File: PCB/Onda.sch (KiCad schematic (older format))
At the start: 0 parts

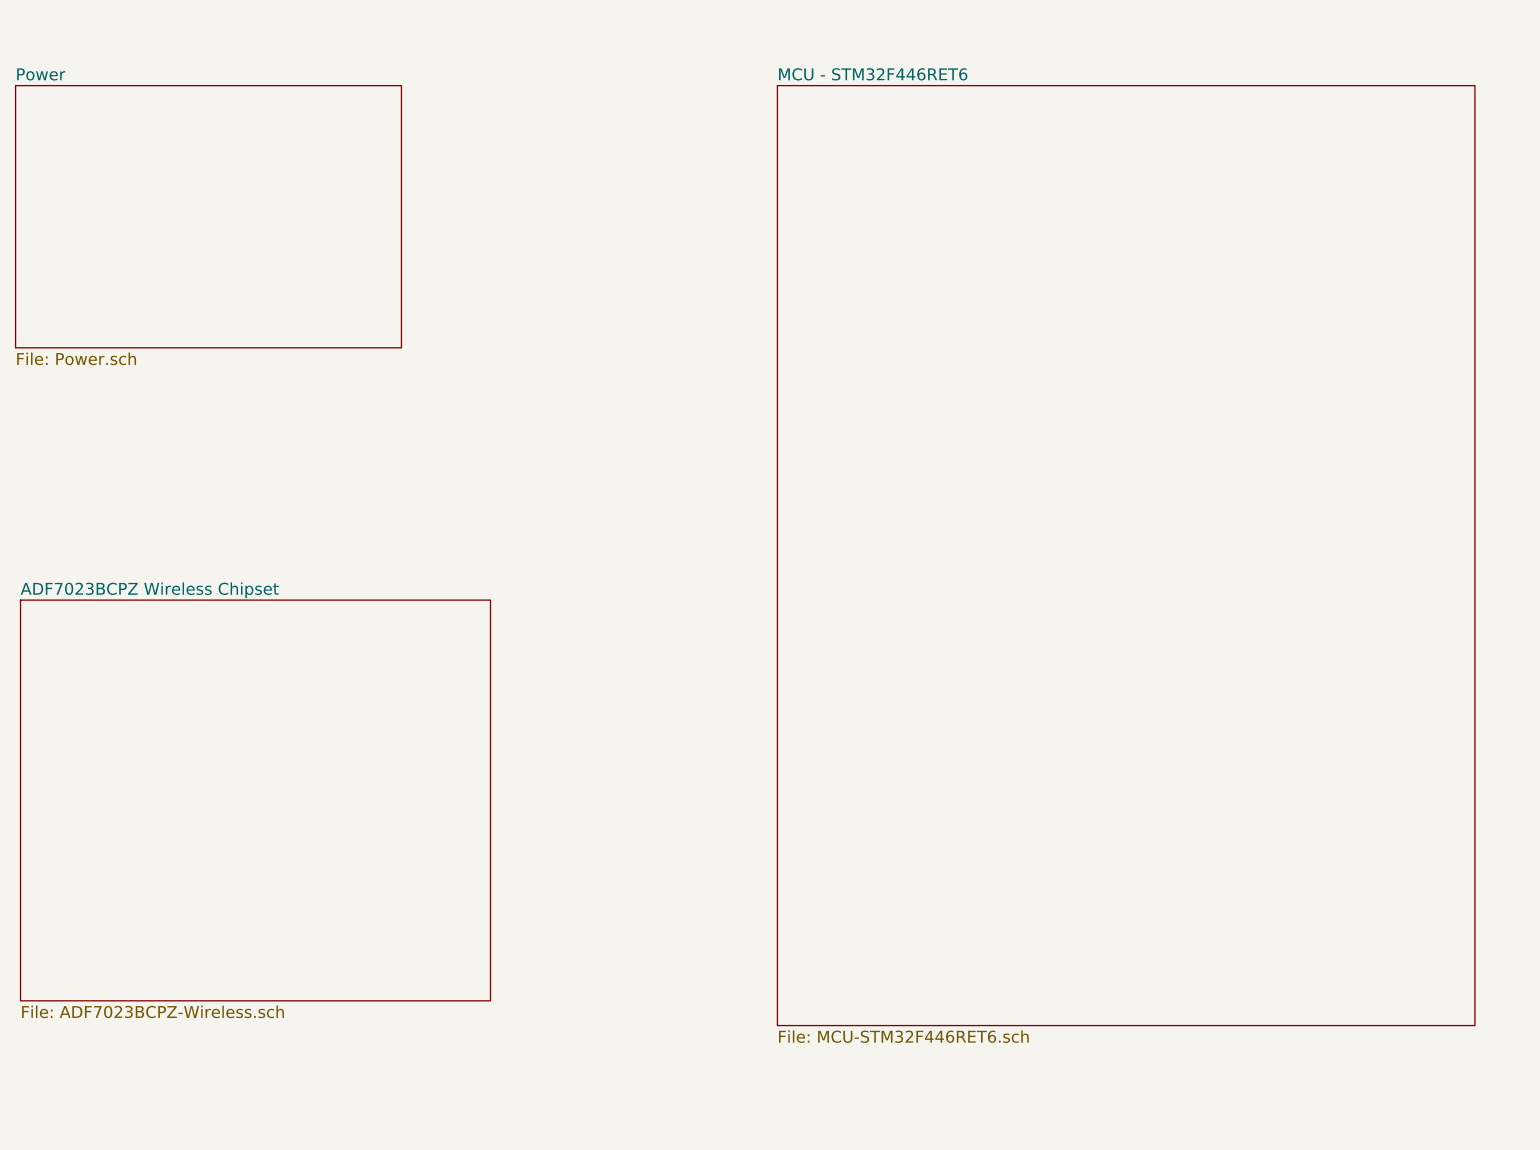
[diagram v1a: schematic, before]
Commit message: Sheets
Hiearchal sheet structure mostly established and linked. Need to
research more on OTA pgoramming with ADF7023 if possible.
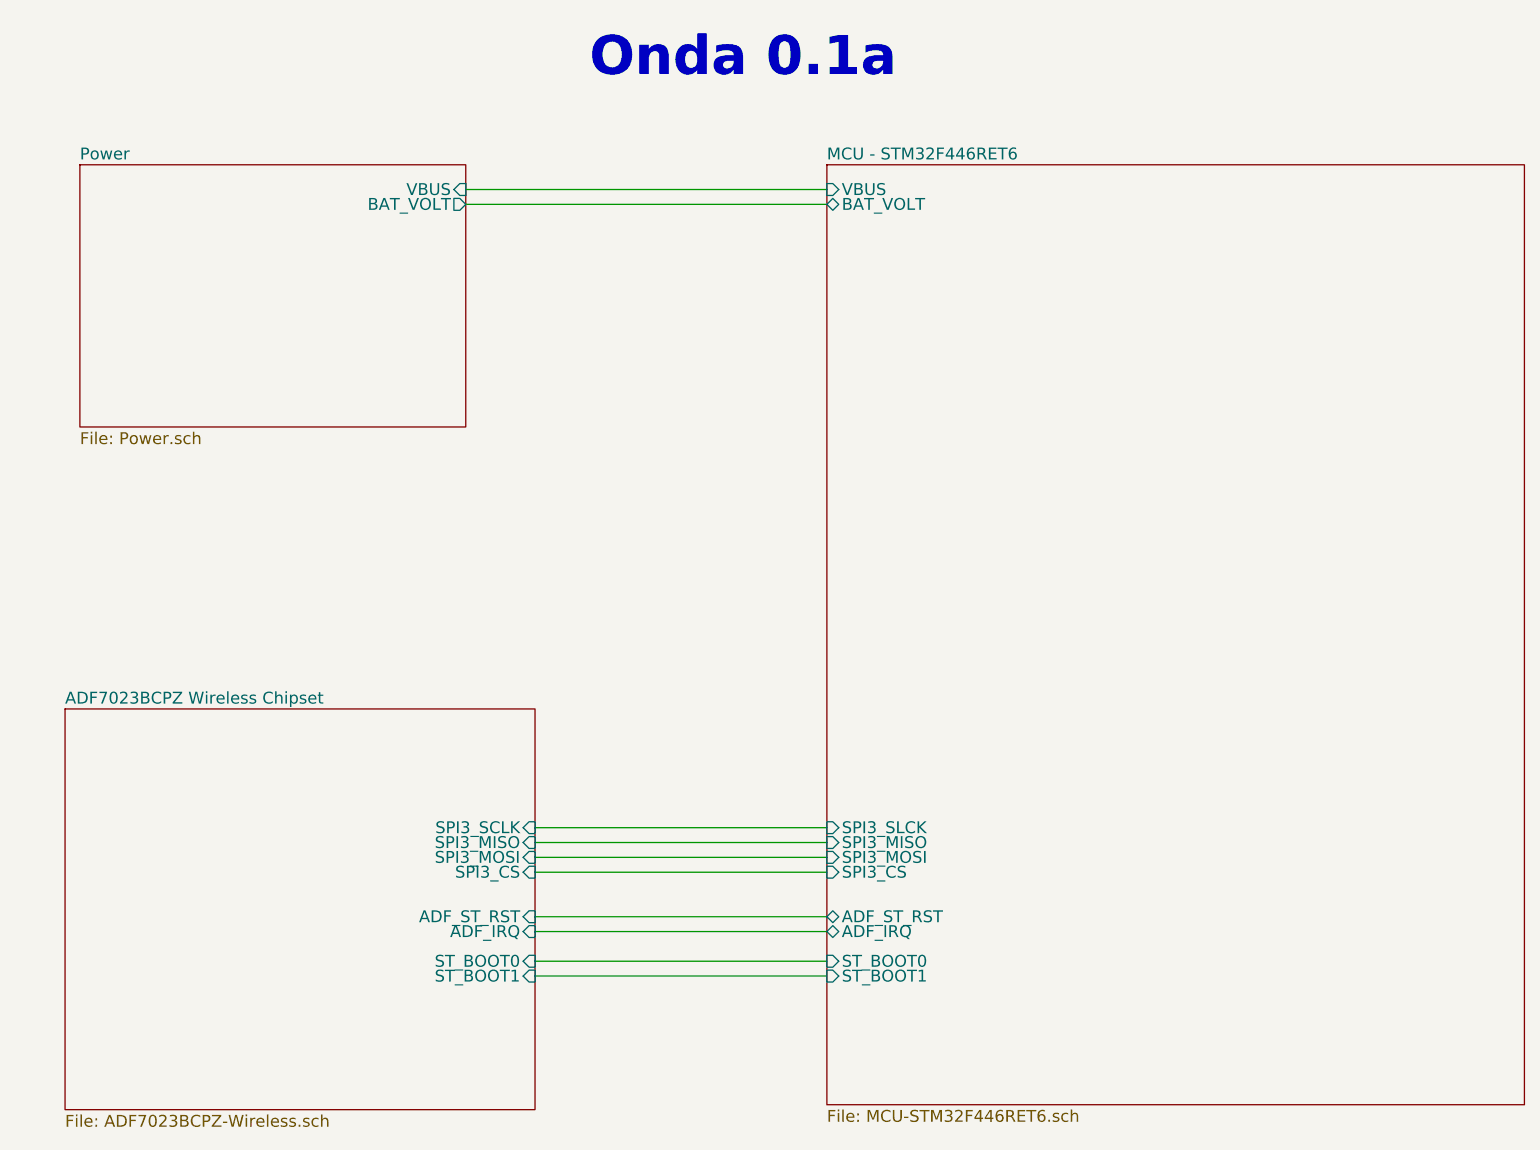
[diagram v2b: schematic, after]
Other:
- note added: "Onda 0.1a"
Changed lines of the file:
@@
 $EndDescr
 $Sheet
-S 1875 1200 1950 1325
+S 2200 1600 1950 1325
 U 5812C70E
 F0 "Power" 60
 F1 "Power.sch" 60
+F2 "VBUS" I R 4150 1725 60
+F3 "BAT_VOLT" O R 4150 1800 60
 $EndSheet
 $Sheet
-S 1900 3800 2375 2025
+S 2125 4350 2375 2025
 U 5812C711
 F0 "ADF7023BCPZ Wireless Chipset" 60
 F1 "ADF7023BCPZ-Wireless.sch" 60
+F2 "SPI3_CS" I R 4500 5175 60
+F3 "SPI3_MOSI" I R 4500 5100 60
+F4 "SPI3_SCLK" I R 4500 4950 60
+F5 "SPI3_MISO" I R 4500 5025 60
+F6 "ADF_IRQ" I R 4500 5475 60
+F7 "ST_BOOT0" I R 4500 5625 60
+F8 "ST_BOOT1" I R 4500 5700 60
+F9 "ADF_ST_RST" I R 4500 5400 60
 $EndSheet
 $Sheet
-S 5725 1200 3525 4750
+S 5975 1600 3525 4750
 U 5812C714
 F0 "MCU - STM32F446RET6" 60
 F1 "MCU-STM32F446RET6.sch" 60
+F2 "ADF_ST_RST" B L 5975 5400 60
+F3 "ADF_IRQ" B L 5975 5475 60
+F4 "VBUS" I L 5975 1725 60
+F6 "ST_BOOT1" I L 5975 5700 60
+F7 "BAT_VOLT" B L 5975 1800 60
+F8 "SPI3_SLCK" I L 5975 4950 60
+F9 "SPI3_MISO" I L 5975 5025 60
+F10 "SPI3_MOSI" I L 5975 5100 60
+F11 "SPI3_CS" I L 5975 5175 60
+F12 "ST_BOOT0" I L 5975 5625 60
 $EndSheet
+Wire Wire Line
+	5975 4950 4500 4950
+Wire Wire Line
+	4500 5025 5975 5025
+Wire Wire Line
+	5975 5100 4500 5100
+Wire Wire Line
+	4500 5175 5975 5175
+Wire Wire Line
+	4500 5400 5975 5400
+Wire Wire Line
+	4500 5475 5975 5475
+Wire Wire Line
+	5975 5625 4500 5625
+Wire Wire Line
+	4500 5700 5975 5700
+Wire Wire Line
+	4150 1725 5975 1725
+Wire Wire Line
+	4150 1800 5975 1800
+Text Notes 4775 1175 0    197  ~ 39
+Onda 0.1a
 $EndSCHEMATC
